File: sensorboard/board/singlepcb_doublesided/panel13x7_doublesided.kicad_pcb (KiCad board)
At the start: 2 copper layers, 200 x 262.1 mm, 190 parts, among them U11 SiPM

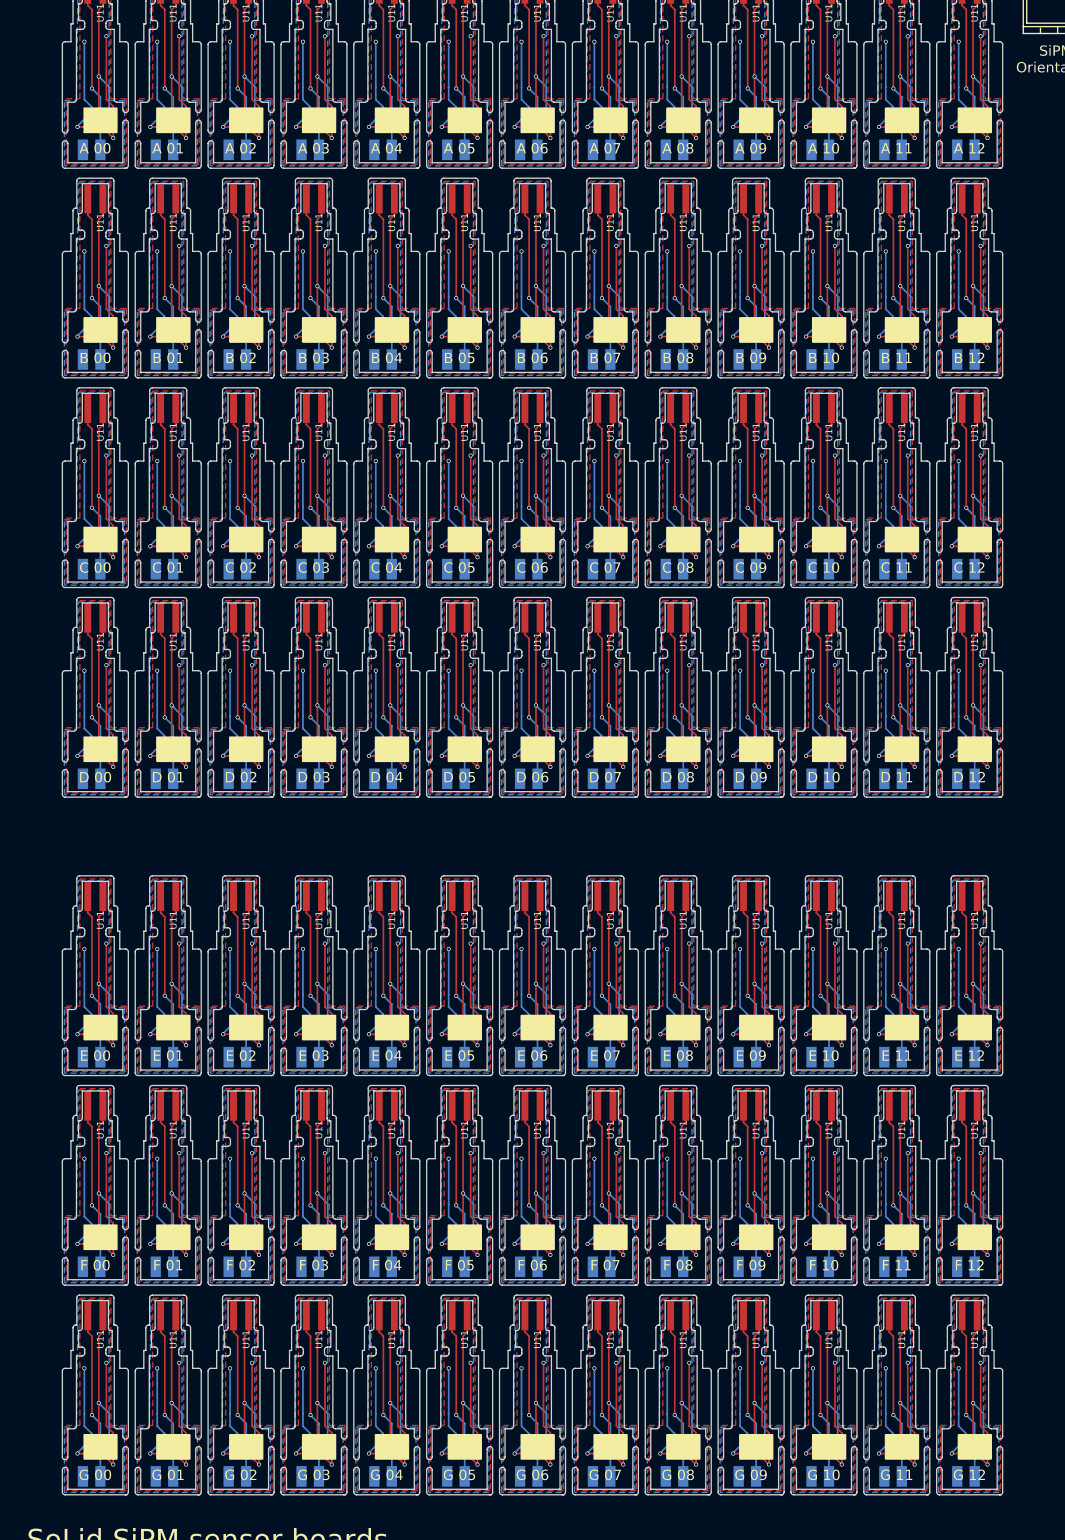
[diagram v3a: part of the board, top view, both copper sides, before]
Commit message: Hopefully easier to cut out.
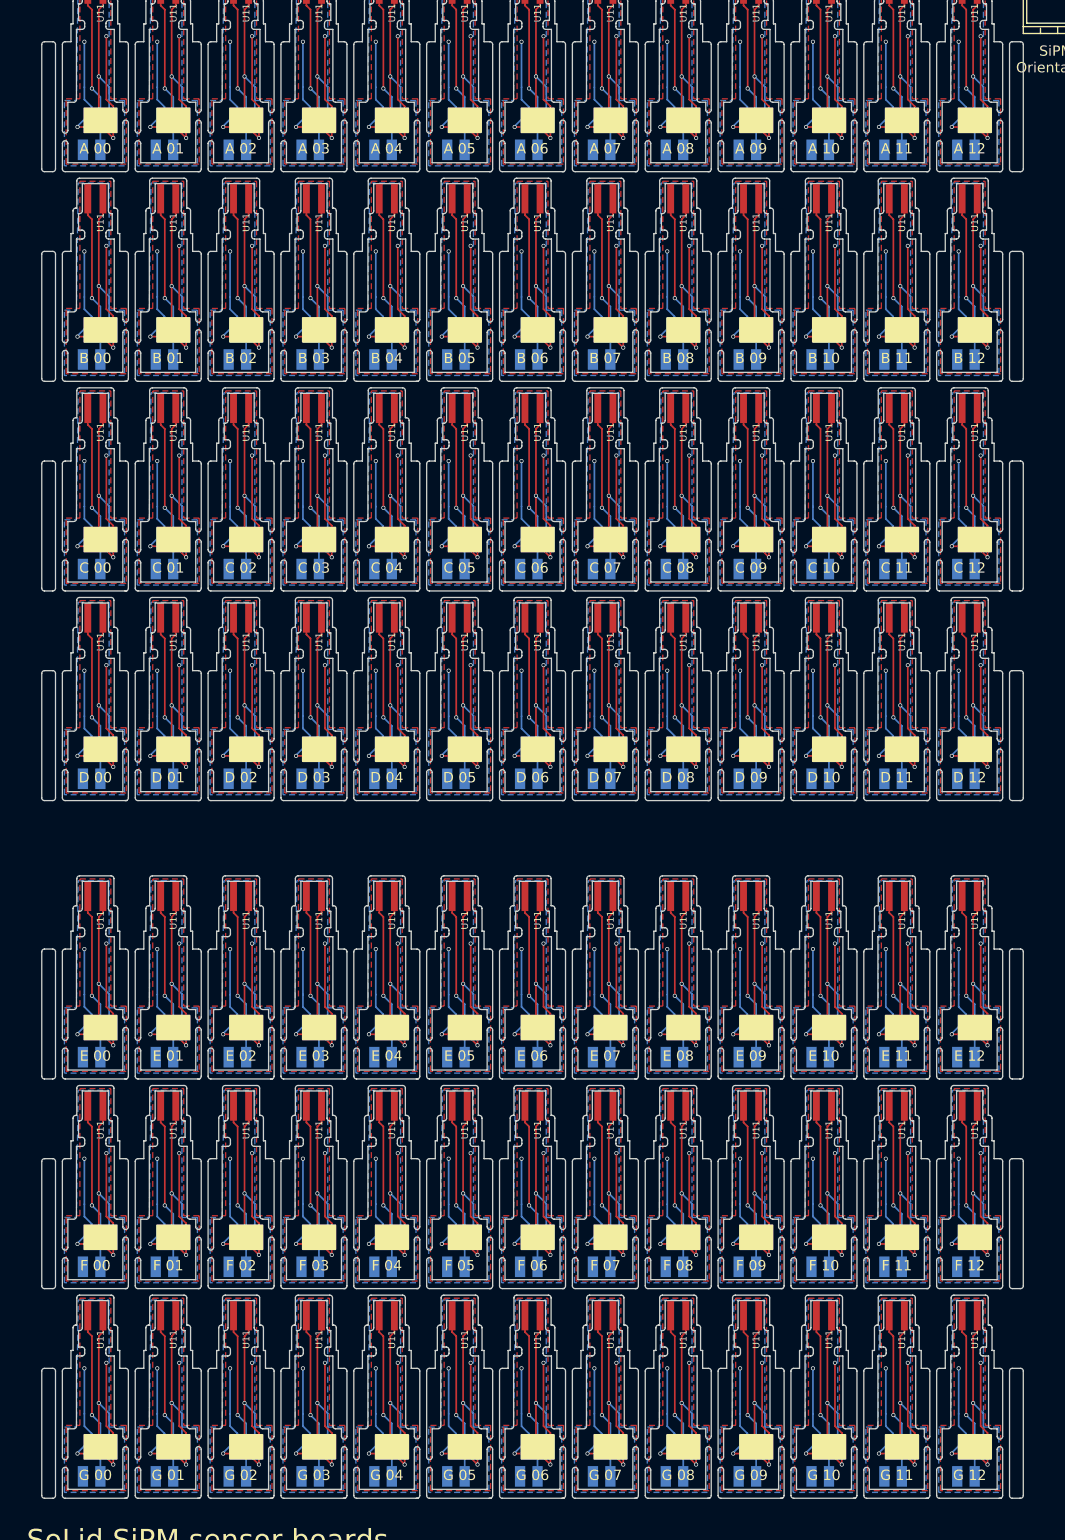
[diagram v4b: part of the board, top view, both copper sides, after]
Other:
- outline, holes or cut-outs redrawn

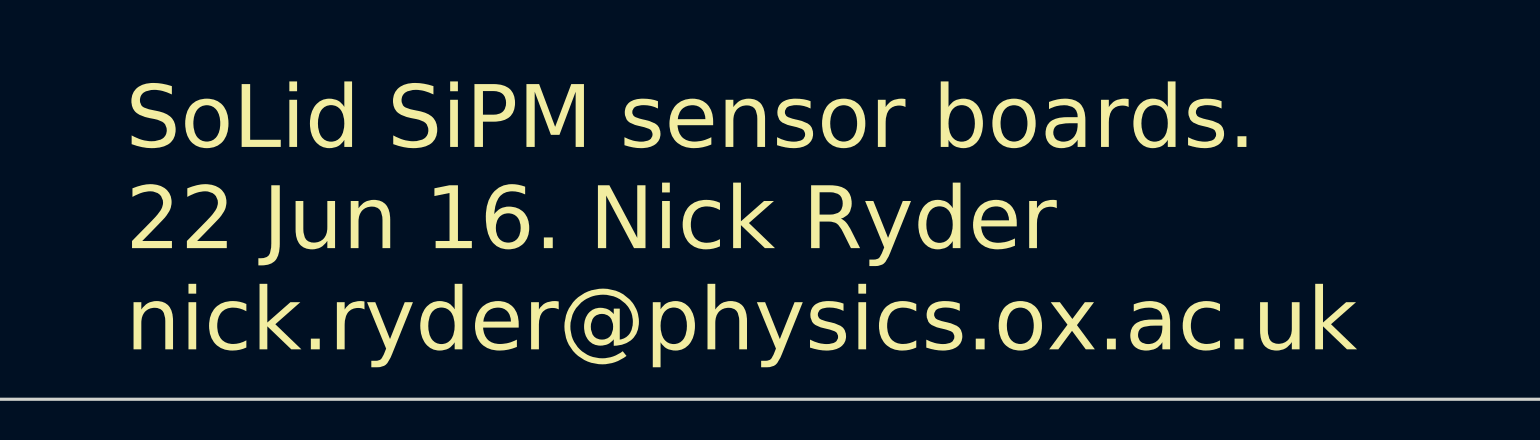
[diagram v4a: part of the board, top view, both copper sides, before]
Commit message: Updated date on silk screen.
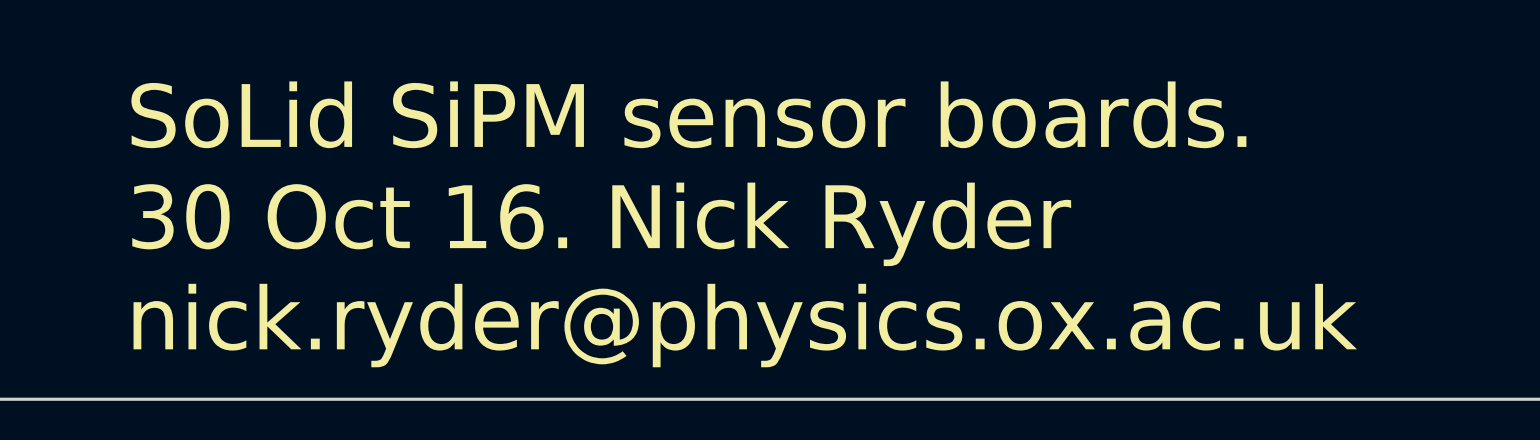
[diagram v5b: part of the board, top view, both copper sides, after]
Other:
- board text added: "SoLid SiPM sensor boards. 30 Oct 16. Nick Ryder nick.ryder@physics.ox.ac.uk"
- board text removed: "SoLid SiPM sensor boards. 22 Jun 16. Nick Ryder nick.ryder@physics.ox.ac.uk"
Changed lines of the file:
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@@
   )
   (layers
-    (0 F.Cu signal hide)
-    (31 B.Cu signal hide)
-    (32 B.Adhes user hide)
-    (33 F.Adhes user hide)
-    (34 B.Paste user hide)
-    (35 F.Paste user hide)
-    (36 B.SilkS user hide)
-    (37 F.SilkS user hide)
-    (38 B.Mask user hide)
-    (39 F.Mask user hide)
-    (40 Dwgs.User user hide)
-    (41 Cmts.User user hide)
-    (42 Eco1.User user hide)
-    (43 Eco2.User user hide)
+    (0 F.Cu signal)
+    (31 B.Cu signal)
+    (32 B.Adhes user)
+    (33 F.Adhes user)
+    (34 B.Paste user)
+    (35 F.Paste user)
+    (36 B.SilkS user)
+    (37 F.SilkS user)
+    (38 B.Mask user)
+    (39 F.Mask user)
+    (40 Dwgs.User user)
+    (41 Cmts.User user)
+    (42 Eco1.User user)
+    (43 Eco2.User user)
     (44 Edge.Cuts user)
-    (45 Margin user hide)
-    (46 B.CrtYd user hide)
-    (47 F.CrtYd user hide)
-    (48 B.Fab user hide)
-    (49 F.Fab user hide)
+    (45 Margin user)
+    (46 B.CrtYd user)
+    (47 F.CrtYd user)
+    (48 B.Fab user)
+    (49 F.Fab user)
   )
   (setup
@@
     (pad_to_mask_clearance 0.2)
     (aux_axis_origin 17.5 280.25)
-    (visible_elements FFFFF601)
+    (visible_elements FFFFFFFF)
     (pcbplotparams
       (layerselection 0x3d0fc_80000001)
@@
   (gr_line (start 187.5 27.5) (end 187.5 35) (layer F.SilkS) (width 0.2))
   (gr_line (start 180 27.5) (end 187.5 27.5) (layer F.SilkS) (width 0.2))
-  (gr_text "SoLid SiPM sensor boards. \n22 Jun 16. Nick Ryder\nnick.ryder@physics.ox.ac.uk" (at 35 260) (layer F.SilkS)
+  (gr_text "SoLid SiPM sensor boards. \n30 Oct 16. Nick Ryder\nnick.ryder@physics.ox.ac.uk" (at 35 260) (layer F.SilkS)
     (effects (font (size 3 3) (thickness 0.3)) (justify left))
   )

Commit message: Removed unwated labels on SiPM PCB.
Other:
- outline, holes or cut-outs redrawn
